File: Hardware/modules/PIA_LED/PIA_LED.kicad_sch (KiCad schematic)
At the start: 37 parts, among them J1 Bus_PCI_6502, J2 PIA_A, J3 PIA_B, U1 6520, U2 74HC138

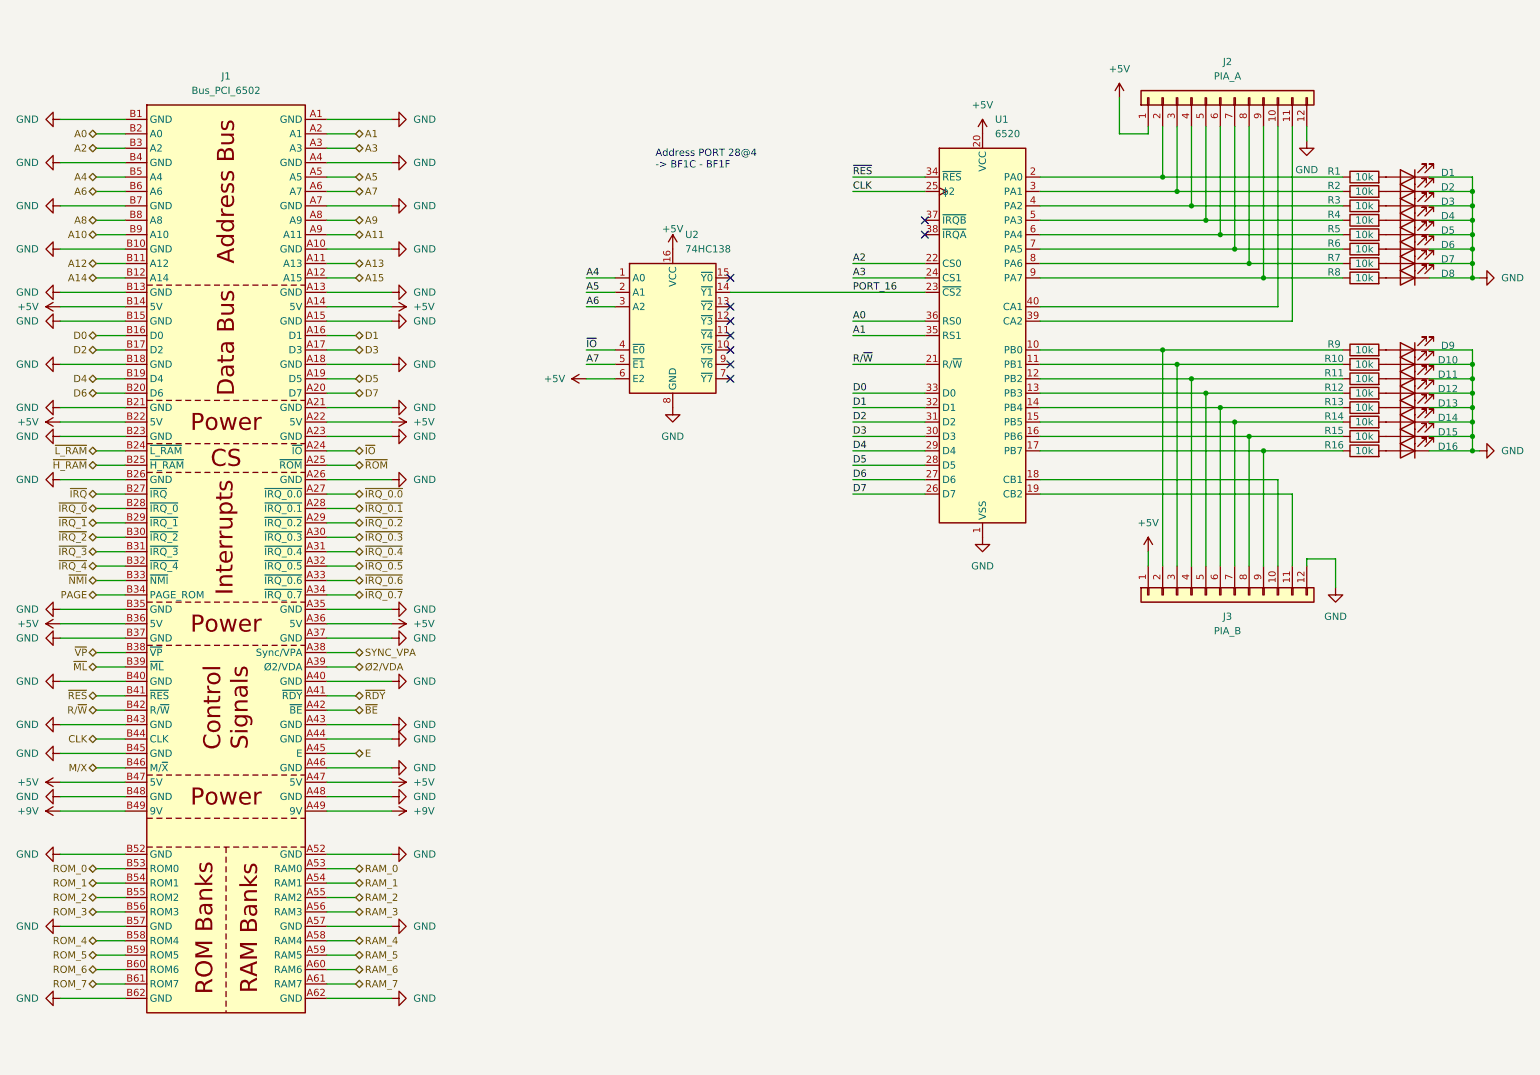
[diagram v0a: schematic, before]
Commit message: Hardware Update Add MyCPU VGA Module Beautify all Schematics minor Error corrections Readme Update
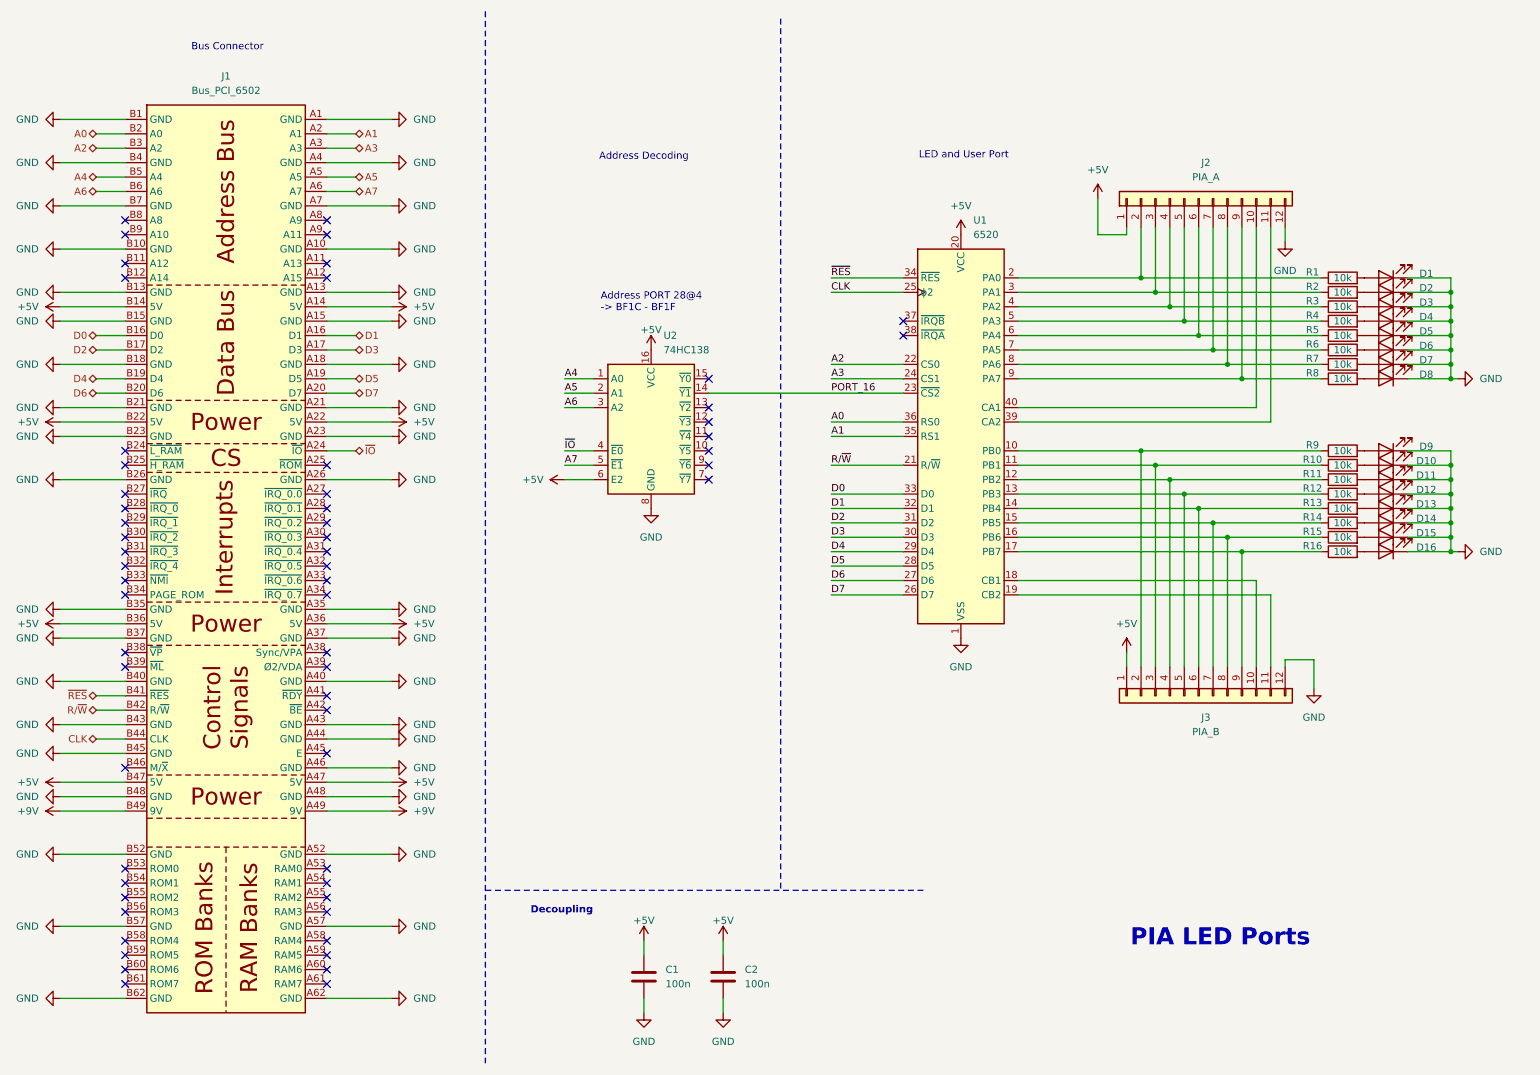
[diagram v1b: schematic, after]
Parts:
- added C1, C2: 100n, Capacitor_SMD:C_0805_2012Metric, symbol Device:C
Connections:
- net +5V: now also C1.1, C2.1
- net GND: now also C1.2, C2.2
- net A10: no longer names the net of J1.B9 (A10)
- net A11: no longer names the net of J1.A9 (A11)
- net A12: no longer names the net of J1.B11 (A12)
- net A13: no longer names the net of J1.A11 (A13)
- net A14: no longer names the net of J1.B12 (A14)
- net A15: no longer names the net of J1.A12 (A15)
- net A8: no longer names the net of J1.B8 (A8)
- net A9: no longer names the net of J1.A8 (A9)
- net E: no longer names the net of J1.A45 (E)
- net M/X: no longer names the net of J1.B46 (M/~{X})
- net PAGE: no longer names the net of J1.B34 (PAGE_ROM)
- net RAM_0: no longer names the net of J1.A53 (RAM0)
- net RAM_1: no longer names the net of J1.A54 (RAM1)
- net RAM_2: no longer names the net of J1.A55 (RAM2)
- net RAM_3: no longer names the net of J1.A56 (RAM3)
- net RAM_4: no longer names the net of J1.A58 (RAM4)
- net RAM_5: no longer names the net of J1.A59 (RAM5)
- net RAM_6: no longer names the net of J1.A60 (RAM6)
- net RAM_7: no longer names the net of J1.A61 (RAM7)
- net ROM_0: no longer names the net of J1.B53 (ROM0)
- net ROM_1: no longer names the net of J1.B54 (ROM1)
- net ROM_2: no longer names the net of J1.B55 (ROM2)
- net ROM_3: no longer names the net of J1.B56 (ROM3)
- net ROM_4: no longer names the net of J1.B58 (ROM4)
- net ROM_5: no longer names the net of J1.B59 (ROM5)
- net ROM_6: no longer names the net of J1.B60 (ROM6)
- net ROM_7: no longer names the net of J1.B61 (ROM7)
- net SYNC_VPA: no longer names the net of J1.A38 (Sync/VPA)
- net ~{BE}: no longer names the net of J1.A42 (~{BE})
- net ~{H_RAM}: no longer names the net of J1.B25 (~{H_RAM})
- net ~{IRQ_0.0}: no longer names the net of J1.A27 (~{IRQ_0.0})
- net ~{IRQ_0.1}: no longer names the net of J1.A28 (~{IRQ_0.1})
- net ~{IRQ_0.2}: no longer names the net of J1.A29 (~{IRQ_0.2})
- net ~{IRQ_0.3}: no longer names the net of J1.A30 (~{IRQ_0.3})
- net ~{IRQ_0.4}: no longer names the net of J1.A31 (~{IRQ_0.4})
- net ~{IRQ_0.5}: no longer names the net of J1.A32 (~{IRQ_0.5})
- net ~{IRQ_0.6}: no longer names the net of J1.A33 (~{IRQ_0.6})
- net ~{IRQ_0.7}: no longer names the net of J1.A34 (~{IRQ_0.7})
- net ~{IRQ_0}: no longer names the net of J1.B28 (~{IRQ_0})
- net ~{IRQ_1}: no longer names the net of J1.B29 (~{IRQ_1})
- net ~{IRQ_2}: no longer names the net of J1.B30 (~{IRQ_2})
- net ~{IRQ_3}: no longer names the net of J1.B31 (~{IRQ_3})
- net ~{IRQ_4}: no longer names the net of J1.B32 (~{IRQ_4})
- net ~{IRQ}: no longer names the net of J1.B27 (~{IRQ})
- net ~{L_RAM}: no longer names the net of J1.B24 (~{L_RAM})
- net ~{ML}: no longer names the net of J1.B39 (~{ML})
- net ~{NMI}: no longer names the net of J1.B33 (~{NMI})
- net ~{RDY}: no longer names the net of J1.A41 (~{RDY})
- net ~{ROM}: no longer names the net of J1.A25 (~{ROM})
- net ~{VP}: no longer names the net of J1.B38 (~{VP})
- net Ø2/VDA: no longer names the net of J1.A39 (Ø2/VDA)
- no-connect marks 9 -> 60
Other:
- note added: "Address Decoding"
- note added: "Bus Connector"
- note added: "Decoupling"
- note added: "LED and User Port"
- note added: "PIA LED Ports"
- company: (none) -> Synthron
- title: (none) -> S65xx Computer System
- moved on the sheet: D1, D10, D11, D12, D13, D14, D15, D16, D2, D3, D4, D5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

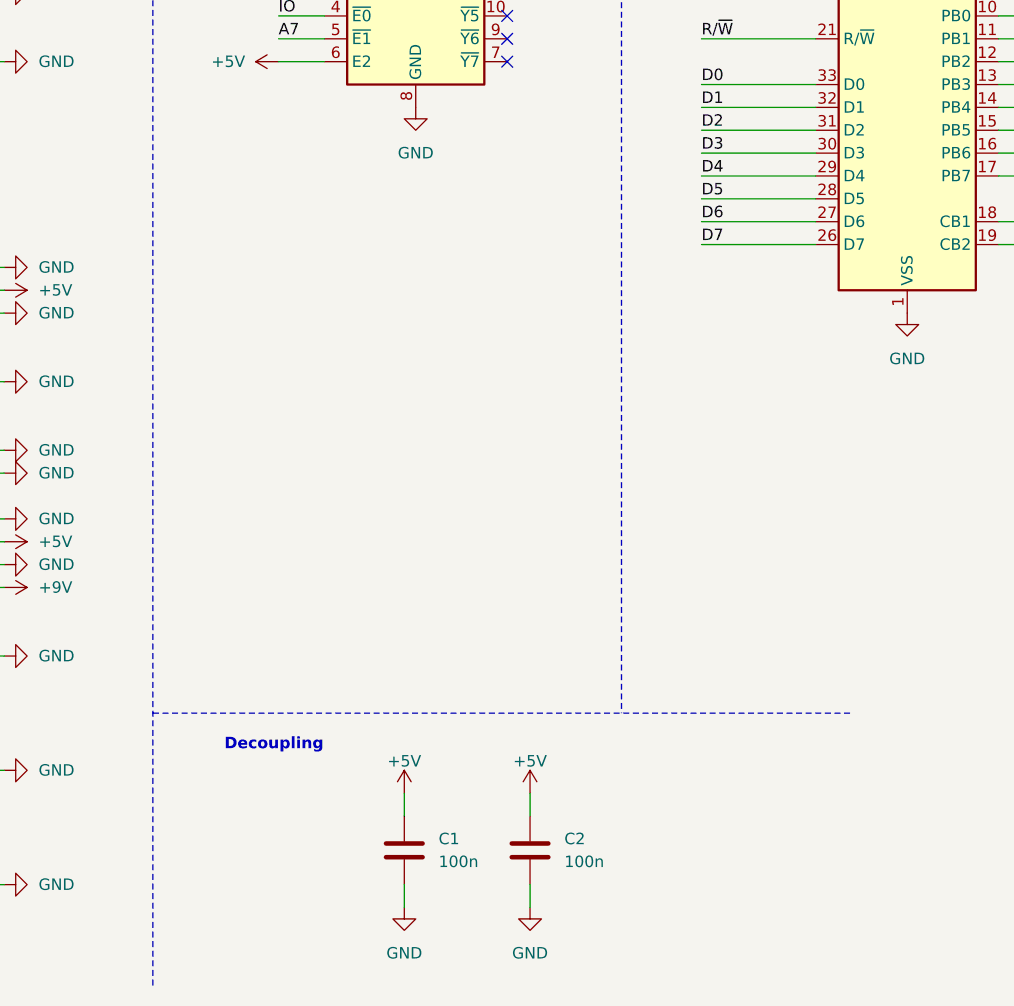
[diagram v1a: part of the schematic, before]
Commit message: Hardware Review Pt. 1 fix Address Decoding for Strobe Generators add bulk capacitance to every board fix wiring of Prototyping Board
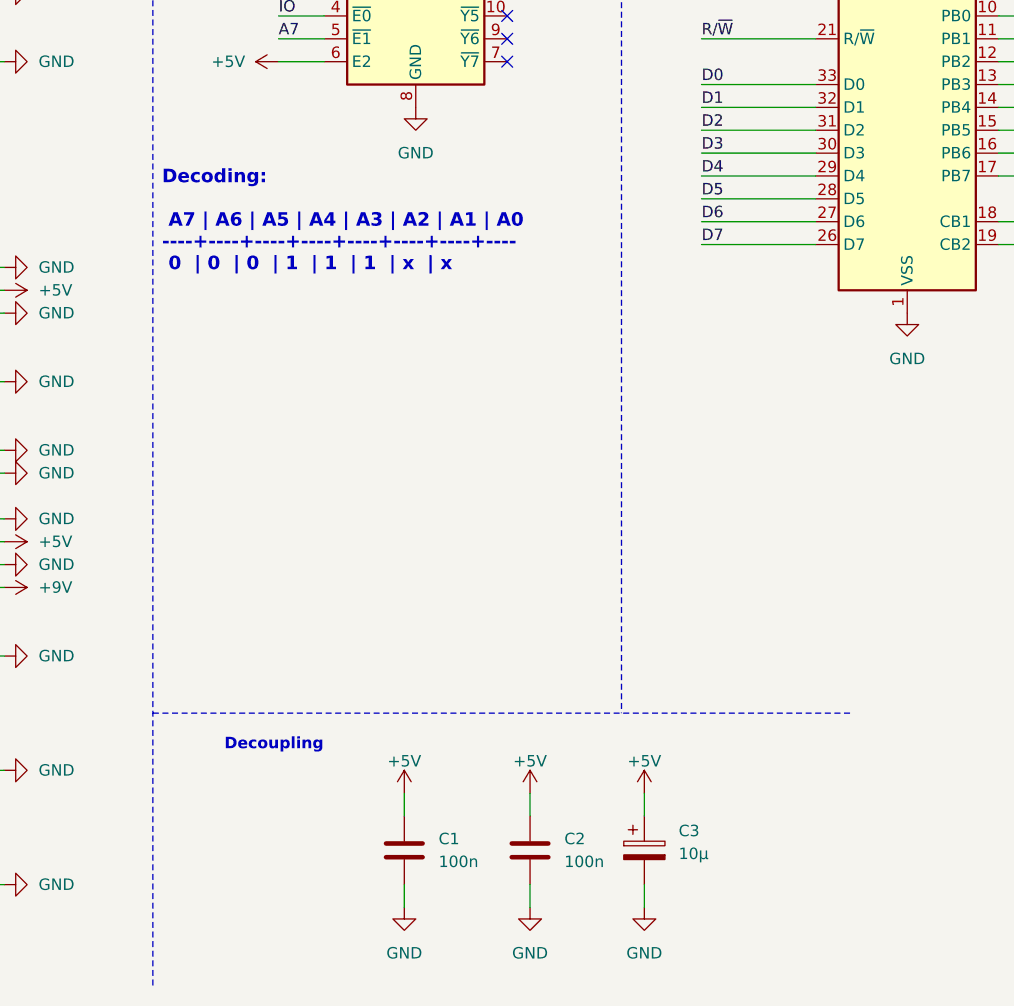
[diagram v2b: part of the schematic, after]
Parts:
- added C3: 10µ, Capacitor_THT:CP_Radial_D5.0mm_P2.50mm, symbol Device:C_Polarized
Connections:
- net +5V: now also C3.1
- net GND: now also C3.2
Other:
- note added: "Decoding: A7 | A6 | A5 | A4 | A3 | A2 | A1 | A0 ----+----+----+----+----+----+----+---- 0 | 0 | 0 | 1 | 1 | 1 | x | x"
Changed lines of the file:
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@@
 	(wire
 		(pts
+			(xy 153.67 175.26) (xy 153.67 177.8)
+		)
+		(stroke
+			(width 0)
+			(type default)
+		)
+	)
+	(wire
+		(pts
 			(xy 24.13 81.28) (xy 35.56 81.28)
 		)
@@
 	(wire
 		(pts
+			(xy 153.67 185.42) (xy 153.67 187.96)
+		)
+		(stroke
+			(width 0)
+			(type default)
+		)
+	)
+	(wire
+		(pts
 			(xy 246.38 106.68) (xy 232.41 106.68)
 		)
@@
 		)
 	)
+	(text "Decoding:\n\n A7 | A6 | A5 | A4 | A3 | A2 | A1 | A0\n----+----+----+----+----+----+----+----\n 0  | 0  | 0  | 1  | 1  | 1  | x  | x"
+		(exclude_from_sim no)
+		(at 100.076 111.76 0)
+		(effects
+			(font
+				(face "DejaVu Sans Mono")
+				(size 1.5 1.5)
+				(thickness 0.254)
+				(bold yes)
+			)
+			(justify left)
+		)
+	)
 	(text "PIA LED Ports"
 		(exclude_from_sim no)
@@
 	)
 	(symbol
+		(lib_id "power:GND")
+		(at 153.67 187.96 0)
+		(mirror y)
+		(unit 1)
+		(exclude_from_sim no)
+		(in_bom yes)
+		(on_board yes)
+		(dnp no)
+		(fields_autoplaced yes)
+		(property "Reference" "#PWR066"
+			(at 153.67 194.31 0)
+			(effects
+				(font
+					(size 1.27 1.27)
+				)
+				(hide yes)
+			)
+		)
+		(property "Value" "GND"
+			(at 153.67 193.04 0)
+			(effects
+				(font
+					(size 1.27 1.27)
+				)
+			)
+		)
+		(property "Footprint" ""
+			(at 153.67 187.96 0)
+			(effects
+				(font
+					(size 1.27 1.27)
+				)
+				(hide yes)
+			)
+		)
+		(property "Datasheet" ""
+			(at 153.67 187.96 0)
+			(effects
+				(font
+					(size 1.27 1.27)
+				)
+				(hide yes)
+			)
+		)
+		(property "Description" "Power symbol creates a global label with name \"GND\" , ground"
+			(at 153.67 187.96 0)
+			(effects
+				(font
+					(size 1.27 1.27)
+				)
+				(hide yes)
+			)
+		)
+		(pin "1"
+		)
+		(instances
+			(project "PIA_LED"
+				(path "/115ae6c9-9ac4-4f12-9a62-daacb6d31443"
+					(reference "#PWR066")
+					(unit 1)
+				)
+			)
+		)
+	)
+	(symbol
 		(lib_id "Device:LED")
 		(at 257.81 63.5 180)
@@
 	)
 	(symbol
+		(lib_id "power:+5V")
+		(at 153.67 175.26 0)
+		(mirror y)
+		(unit 1)
+		(exclude_from_sim no)
+		(in_bom yes)
+		(on_board yes)
+		(dnp no)
+		(property "Reference" "#PWR065"
+			(at 153.67 179.07 0)
+			(effects
+				(font
+					(size 1.27 1.27)
+				)
+				(hide yes)
+			)
+		)
+		(property "Value" "+5V"
+			(at 153.67 171.704 0)
+			(effects
+				(font
+					(size 1.27 1.27)
+				)
+			)
+		)
+		(property "Footprint" ""
+			(at 153.67 175.26 0)
+			(effects
+				(font
+					(size 1.27 1.27)
+				)
+				(hide yes)
+			)
+		)
+		(property "Datasheet" ""
+			(at 153.67 175.26 0)
+			(effects
+				(font
+					(size 1.27 1.27)
+				)
+				(hide yes)
+			)
+		)
+		(property "Description" "Power symbol creates a global label with name \"+5V\""
+			(at 153.67 175.26 0)
+			(effects
+				(font
+					(size 1.27 1.27)
+				)
+				(hide yes)
+			)
+		)
+		(pin "1"
+		)
+		(instances
+			(project "PIA_LED"
+				(path "/115ae6c9-9ac4-4f12-9a62-daacb6d31443"
+					(reference "#PWR065")
+					(unit 1)
+				)
+			)
+		)
+	)
+	(symbol
 		(lib_id "Device:R")
 		(at 250.19 73.66 90)
@@
 					(unit 1)
 				)
+			)
+		)
+	)
+	(symbol
+		(lib_id "Device:C_Polarized")
+		(at 153.67 181.61 0)
+		(unit 1)
+		(exclude_from_sim no)
+		(in_bom yes)
+		(on_board yes)
+		(dnp no)
+		(fields_autoplaced yes)
+		(property "Reference" "C3"
+			(at 157.48 179.4509 0)
+			(effects
+				(font
+					(size 1.27 1.27)
+				)
+				(justify left)
+			)
+		)
+		(property "Value" "10µ"
+			(at 157.48 181.9909 0)
+			(effects
+				(font
+					(size 1.27 1.27)
+				)
+				(justify left)
+			)
+		)
+		(property "Footprint" "Capacitor_THT:CP_Radial_D5.0mm_P2.50mm"
+			(at 154.6352 185.42 0)
+			(effects
+				(font
+					(size 1.27 1.27)
+				)
+				(hide yes)
+			)
+		)
+		(property "Datasheet" "~"
+			(at 153.67 181.61 0)
+			(effects
+				(font
+					(size 1.27 1.27)
+				)
+				(hide yes)
+			)
+		)
+		(property "Description" "Polarized capacitor"
+			(at 153.67 181.61 0)
+			(effects
+				(font
+					(size 1.27 1.27)
+				)
+				(hide yes)
+			)
+		)
+		(pin "1"
+		)
+		(pin "2"
+		)
+		(instances
+			(project ""
+				(path "/115ae6c9-9ac4-4f12-9a62-daacb6d31443"
+					(reference "C3")
+					(unit 1)
+				)
